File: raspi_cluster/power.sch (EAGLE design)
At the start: 5 parts

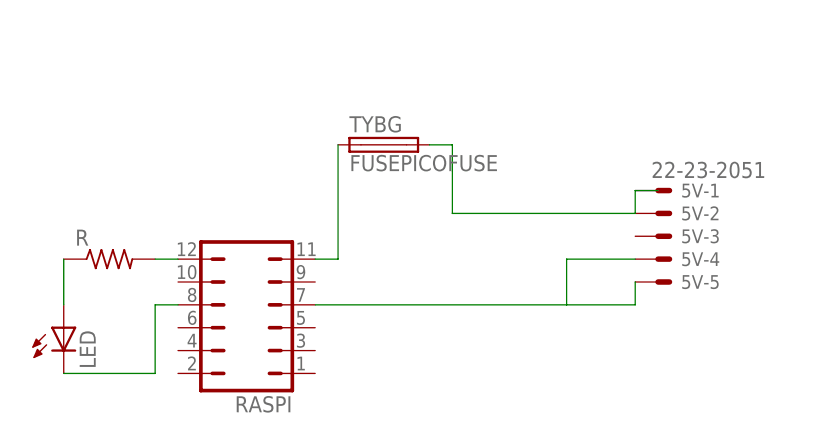
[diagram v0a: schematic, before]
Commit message: updated power schematic for breakout board
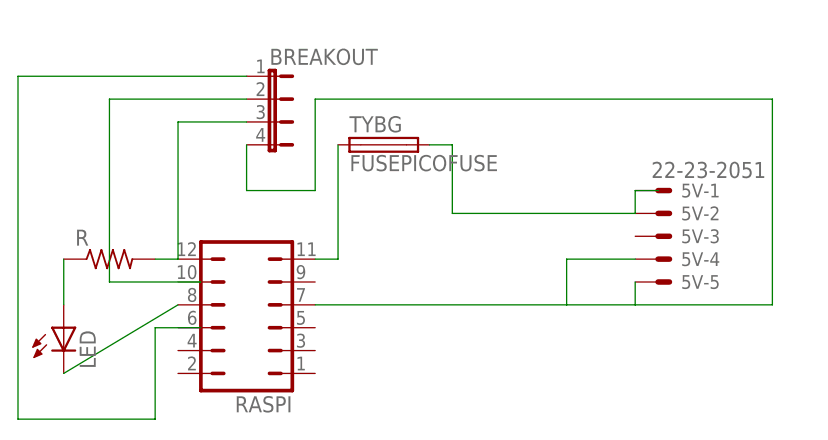
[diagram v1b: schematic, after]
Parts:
- added BREAKOUT: (no value), jumper:JP4E
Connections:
- new net N$4: BREAKOUT.1
- new net N$7: BREAKOUT.2
- net N$2: now also BREAKOUT.3
- net N$6: now also BREAKOUT.4
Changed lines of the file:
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@@
 <part name="5V" library="con-molex" deviceset="22-23-2051" device=""/>
 <part name="R" library="resistor" deviceset="R-US_" device="0204/7"/>
+<part name="BREAKOUT" library="jumper" deviceset="JP4E" device=""/>
 </parts>
 <sheets>
@@
 <instance part="5V" gate="-5" x="129.54" y="50.8"/>
 <instance part="R" gate="G$1" x="68.58" y="53.34"/>
+<instance part="BREAKOUT" gate="G$1" x="86.36" y="71.12" rot="R270"/>
 </instances>
 <busses>
@@
 <net name="N$4" class="0">
 <segment>
-<pinref part="LED" gate="G$1" pin="C"/>
-<wire x1="63.5" y1="40.64" x2="73.66" y2="40.64" width="0.1524" layer="91"/>
-<wire x1="73.66" y1="40.64" x2="73.66" y2="48.26" width="0.1524" layer="91"/>
-<pinref part="RASPI" gate="B" pin="8"/>
-<wire x1="76.2" y1="48.26" x2="73.66" y2="48.26" width="0.1524" layer="91"/>
+<pinref part="BREAKOUT" gate="G$1" pin="1"/>
+<wire x1="83.82" y1="73.66" x2="58.42" y2="73.66" width="0.1524" layer="91"/>
+<wire x1="58.42" y1="73.66" x2="58.42" y2="35.56" width="0.1524" layer="91"/>
+<wire x1="58.42" y1="35.56" x2="73.66" y2="35.56" width="0.1524" layer="91"/>
+<wire x1="73.66" y1="35.56" x2="73.66" y2="45.72" width="0.1524" layer="91"/>
+<wire x1="73.66" y1="45.72" x2="78.74" y2="45.72" width="0.1524" layer="91"/>
 </segment>
 </net>
@@
 <wire x1="91.44" y1="48.26" x2="119.38" y2="48.26" width="0.1524" layer="91"/>
 <wire x1="119.38" y1="48.26" x2="119.38" y2="53.34" width="0.1524" layer="91"/>
+<wire x1="127" y1="48.26" x2="142.24" y2="48.26" width="0.1524" layer="91"/>
+<wire x1="142.24" y1="48.26" x2="142.24" y2="71.12" width="0.1524" layer="91"/>
+<wire x1="142.24" y1="71.12" x2="91.44" y2="71.12" width="0.1524" layer="91"/>
+<wire x1="91.44" y1="71.12" x2="91.44" y2="60.96" width="0.1524" layer="91"/>
+<pinref part="BREAKOUT" gate="G$1" pin="4"/>
+<wire x1="91.44" y1="60.96" x2="83.82" y2="60.96" width="0.1524" layer="91"/>
+<wire x1="83.82" y1="60.96" x2="83.82" y2="66.04" width="0.1524" layer="91"/>
 </segment>
 </net>
@@
 <pinref part="R" gate="G$1" pin="2"/>
 <wire x1="76.2" y1="53.34" x2="73.66" y2="53.34" width="0.1524" layer="91"/>
+<pinref part="BREAKOUT" gate="G$1" pin="3"/>
+<wire x1="83.82" y1="68.58" x2="76.2" y2="68.58" width="0.1524" layer="91"/>
+<wire x1="76.2" y1="68.58" x2="76.2" y2="53.34" width="0.1524" layer="91"/>
 </segment>
 </net>
+<net name="N$7" class="0">
+<segment>
+<pinref part="BREAKOUT" gate="G$1" pin="2"/>
+<wire x1="83.82" y1="71.12" x2="68.58" y2="71.12" width="0.1524" layer="91"/>
+<wire x1="68.58" y1="71.12" x2="68.58" y2="50.8" width="0.1524" layer="91"/>
+<wire x1="68.58" y1="50.8" x2="78.74" y2="50.8" width="0.1524" layer="91"/>
+</segment>
+</net>
+<net name="N$8" class="0">
+<segment>
+<pinref part="RASPI" gate="B" pin="8"/>
+<pinref part="LED" gate="G$1" pin="C"/>
+<wire x1="63.5" y1="40.64" x2="76.2" y2="48.26" width="0.1524" layer="91"/>
+</segment>
+</net>

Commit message: New powerboard break out
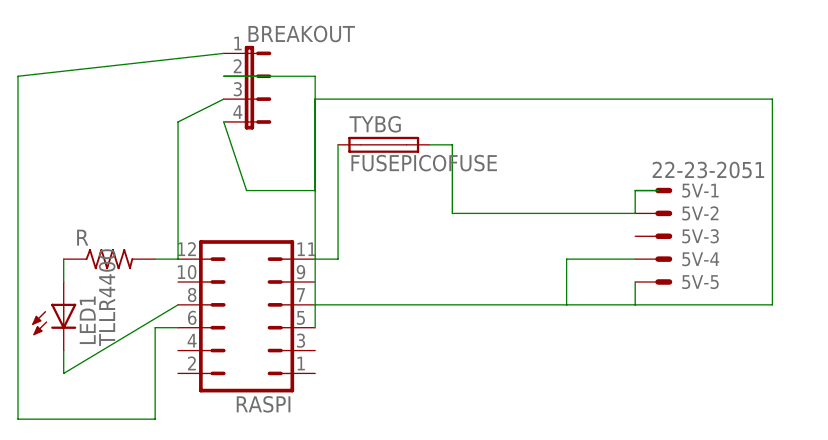
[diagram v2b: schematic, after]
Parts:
- removed LED: (no value), eagle-ltspice:LED_ELD260
- added LED1: TLLR4400, led:TLLR4400
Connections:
- net N$3: now also LED1.A; no longer LED.A
- net N$4: now also RASPI.6
- net N$7: now also RASPI.5
- net N$8: now also LED1.C; no longer LED.C
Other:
- moved on the sheet: BREAKOUT
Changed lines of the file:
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@@
 <parts>
 <part name="RASPI" library="jumper" deviceset="JP6Q" device=""/>
-<part name="LED" library="eagle-ltspice" deviceset="LED_E" device="LD260"/>
 <part name="TYBG" library="fuse" deviceset="FUSE" device="PICOFUSE"/>
 <part name="5V" library="con-molex" deviceset="22-23-2051" device=""/>
 <part name="R" library="resistor" deviceset="R-US_" device="0204/7"/>
 <part name="BREAKOUT" library="jumper" deviceset="JP4E" device=""/>
+<part name="LED1" library="led" deviceset="TLLR4400" device=""/>
 </parts>
 <sheets>
@@
 <instances>
 <instance part="RASPI" gate="B" x="83.82" y="48.26" rot="R90"/>
-<instance part="LED" gate="G$1" x="63.5" y="45.72"/>
 <instance part="TYBG" gate="G$1" x="99.06" y="66.04"/>
 <instance part="5V" gate="-1" x="129.54" y="60.96"/>
@@
 <instance part="5V" gate="-5" x="129.54" y="50.8"/>
 <instance part="R" gate="G$1" x="68.58" y="53.34"/>
-<instance part="BREAKOUT" gate="G$1" x="86.36" y="71.12" rot="R270"/>
+<instance part="BREAKOUT" gate="G$1" x="83.82" y="73.66" rot="R270"/>
+<instance part="LED1" gate="G$1" x="63.5" y="48.26"/>
 </instances>
 <busses>
@@
 </segment>
 </net>
-<net name="N$3" class="0">
-<segment>
-<pinref part="LED" gate="G$1" pin="A"/>
-<wire x1="63.5" y1="48.26" x2="63.5" y2="53.34" width="0.1524" layer="91"/>
-<pinref part="R" gate="G$1" pin="1"/>
-</segment>
-</net>
 <net name="N$4" class="0">
 <segment>
 <pinref part="BREAKOUT" gate="G$1" pin="1"/>
-<wire x1="83.82" y1="73.66" x2="58.42" y2="73.66" width="0.1524" layer="91"/>
+<wire x1="81.28" y1="76.2" x2="58.42" y2="73.66" width="0.1524" layer="91"/>
 <wire x1="58.42" y1="73.66" x2="58.42" y2="35.56" width="0.1524" layer="91"/>
 <wire x1="58.42" y1="35.56" x2="73.66" y2="35.56" width="0.1524" layer="91"/>
 <wire x1="73.66" y1="35.56" x2="73.66" y2="45.72" width="0.1524" layer="91"/>
-<wire x1="73.66" y1="45.72" x2="78.74" y2="45.72" width="0.1524" layer="91"/>
+<pinref part="RASPI" gate="B" pin="6"/>
+<wire x1="73.66" y1="45.72" x2="76.2" y2="45.72" width="0.1524" layer="91"/>
 </segment>
 </net>
@@
 <pinref part="BREAKOUT" gate="G$1" pin="4"/>
 <wire x1="91.44" y1="60.96" x2="83.82" y2="60.96" width="0.1524" layer="91"/>
-<wire x1="83.82" y1="60.96" x2="83.82" y2="66.04" width="0.1524" layer="91"/>
+<wire x1="83.82" y1="60.96" x2="81.28" y2="68.58" width="0.1524" layer="91"/>
 </segment>
 </net>
@@
 <wire x1="76.2" y1="53.34" x2="73.66" y2="53.34" width="0.1524" layer="91"/>
 <pinref part="BREAKOUT" gate="G$1" pin="3"/>
-<wire x1="83.82" y1="68.58" x2="76.2" y2="68.58" width="0.1524" layer="91"/>
+<wire x1="81.28" y1="71.12" x2="76.2" y2="68.58" width="0.1524" layer="91"/>
 <wire x1="76.2" y1="68.58" x2="76.2" y2="53.34" width="0.1524" layer="91"/>
+</segment>
+</net>
+<net name="N$8" class="0">
+<segment>
+<pinref part="RASPI" gate="B" pin="8"/>
+<wire x1="63.5" y1="40.64" x2="76.2" y2="48.26" width="0.1524" layer="91"/>
+<pinref part="LED1" gate="G$1" pin="C"/>
+<wire x1="63.5" y1="43.18" x2="63.5" y2="40.64" width="0.1524" layer="91"/>
+</segment>
+</net>
+<net name="N$3" class="0">
+<segment>
+<pinref part="R" gate="G$1" pin="1"/>
+<pinref part="LED1" gate="G$1" pin="A"/>
+<wire x1="63.5" y1="53.34" x2="63.5" y2="50.8" width="0.1524" layer="91"/>
 </segment>
 </net>
@@
 <segment>
 <pinref part="BREAKOUT" gate="G$1" pin="2"/>
-<wire x1="83.82" y1="71.12" x2="68.58" y2="71.12" width="0.1524" layer="91"/>
-<wire x1="68.58" y1="71.12" x2="68.58" y2="50.8" width="0.1524" layer="91"/>
-<wire x1="68.58" y1="50.8" x2="78.74" y2="50.8" width="0.1524" layer="91"/>
+<pinref part="RASPI" gate="B" pin="5"/>
+<wire x1="81.28" y1="73.66" x2="91.44" y2="73.66" width="0.1524" layer="91"/>
+<wire x1="91.44" y1="73.66" x2="91.44" y2="45.72" width="0.1524" layer="91"/>
 </segment>
 </net>
-<net name="N$8" class="0">
-<segment>
-<pinref part="RASPI" gate="B" pin="8"/>
-<pinref part="LED" gate="G$1" pin="C"/>
-<wire x1="63.5" y1="40.64" x2="76.2" y2="48.26" width="0.1524" layer="91"/>
-</segment>
-</net>
